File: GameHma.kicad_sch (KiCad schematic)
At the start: 14 parts, among them J1 Screw_Terminal_01x02, J2 Motor_Terminal_01x04, J3 Motor_Terminal_01x04, J4 Motor_Terminal_01x04, J5 Motor_Terminal_01x04, U1 ESP32-DEVKIT-V1, U2 A4988_STEPPER_MOTOR_DRIVER_CA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, U3 A4988_STEPPER_MOTOR_DRIVER_CA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, U4 A4988_STEPPER_MOTOR_DRIVER_CA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, U5 A4988_STEPPER_MOTOR_DRIVER_CA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

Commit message: example of how it's done done done
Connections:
- net Ground: no longer C2.2, J1.2 (Pin_2), U3.15 (GND), U3.9 (GND)
- net Vcc: no longer C2.1, J1.1 (Pin_1), U3.16 (VMOT)
- net at U1.1 (3V3), U2.10 (VDD), U4.10 (VDD)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: no longer U3.10 (VDD)
- net at U1.26 (D14), U2.7 (STEP): now also U1.22 (D33)
- net GND: now reaches U3.1 (~{ENABLE})
- net GND: now also C2.2, J1.2 (Pin_2), U3.15 (GND), U3.9 (GND)
- net at U3.11 (1B): now also J3.2 (Pin_2); no longer J3.1 (Pin_1)
- net at U3.12 (1A): now also J3.1 (Pin_1); no longer J3.3 (Pin_3)
- net at U3.13 (2A): now also J3.3 (Pin_3); no longer J3.2 (Pin_2)
- net +V_{DD}: now reaches U3.2 (MS1)
- net +V_{DD}: now also U3.10 (VDD), U3.3 (MS2), U3.4 (MS3)
- net at U1.23 (D25): no longer U3.7 (STEP)
- net DIR_1: now reaches U3.8 (DIR)
- net DIR_1: no longer U1.22 (D33)
- new net +V_{batt}: C2.1, J1.1 (Pin_1), U3.16 (VMOT)
- new net STEP_1: U3.7 (STEP)
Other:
- moved on the sheet: C2, J1, J3, U3

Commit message: nothing
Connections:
- net Ground is gone; now on net GND: C1.2, C3.2, C4.2, U1.2 (GND), U1.29 (GND), U2.15 (GND), U2.9 (GND), U4.15 (GND), U4.9 (GND), U5.15 (GND), U5.9 (GND)
- net +V_{DD}: now also U1.1 (3V3), U2.10 (VDD), U2.2 (MS1), U2.3 (MS2), U2.4 (MS3), U4.10 (VDD), U4.2 (MS1), U4.3 (MS2), U4.4 (MS3), U5.10 (VDD), U5.2 (MS1), U5.3 (MS2), U5.4 (MS3)
- net +V_{batt}: now also C1.1, C3.1, C4.1, U2.16 (VMOT), U4.16 (VMOT), U5.16 (VMOT)
- net DIR_1: now also U1.25 (D27)
- net GND: now also U2.1 (~{ENABLE}), U4.1 (~{ENABLE}), U5.1 (~{ENABLE})
- net STEP_1: now also U1.26 (D14)
- net at U2.11 (1B): now also J2.2 (Pin_2); no longer J2.1 (Pin_1)
- net at U2.13 (2A): now also J2.3 (Pin_3); no longer J2.2 (Pin_2)
- net at U2.12 (1A): now also J2.1 (Pin_1); no longer J2.3 (Pin_3)
- net DIR_2: now reaches U2.8 (DIR)
- net DIR_2: now also U1.22 (D33); no longer U1.25 (D27)
- net at J5.1 (Pin_1): now also U5.12 (1A); no longer U5.11 (1B)
- net at J5.3 (Pin_3): now also U5.13 (2A); no longer U5.12 (1A)
- net at J5.2 (Pin_2): now also U5.11 (1B); no longer U5.13 (2A)
- net STEP_4: now reaches U1.8 (D5), U5.7 (STEP)
- net DIR_4: now reaches U1.5 (D4), U5.8 (DIR)
- net DIR_3: now reaches U1.10 (D19), U4.8 (DIR)
- net STEP_2: now reaches U1.23 (D25)
- net STEP_2: now also U2.7 (STEP)
- net STEP_3: now reaches U1.9 (D18), U4.7 (STEP)
- net at J4.1 (Pin_1): now also U4.12 (1A); no longer U4.11 (1B)
- net at J4.2 (Pin_2): now also U4.11 (1B); no longer U4.13 (2A)
- net at J4.3 (Pin_3): now also U4.13 (2A); no longer U4.12 (1A)
- removed net Vcc: C1.1, C3.1, C4.1, U1.30 (VIN), U2.16 (VMOT), U4.16 (VMOT), U5.16 (VMOT)
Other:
- moved on the sheet: C2, J1, J3, U3

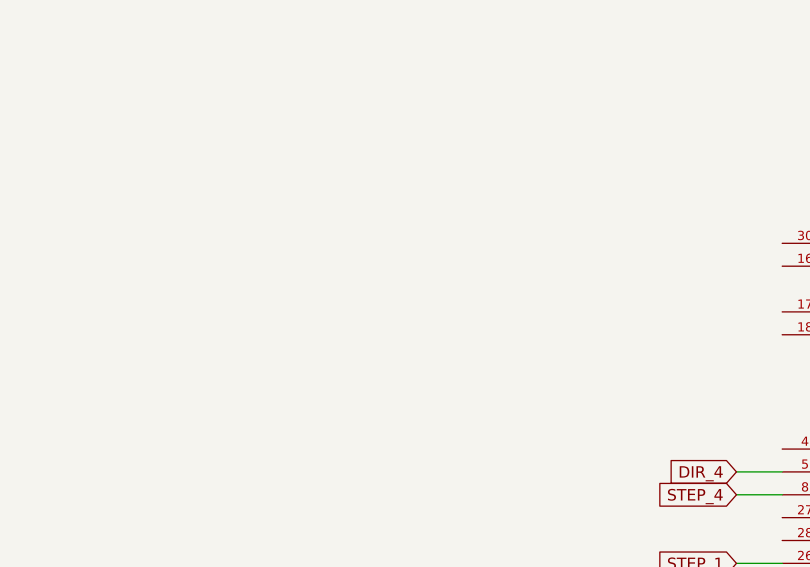
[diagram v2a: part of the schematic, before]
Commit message: create and build SRT_MP1584EN symbol library, add MP1584 in schematic
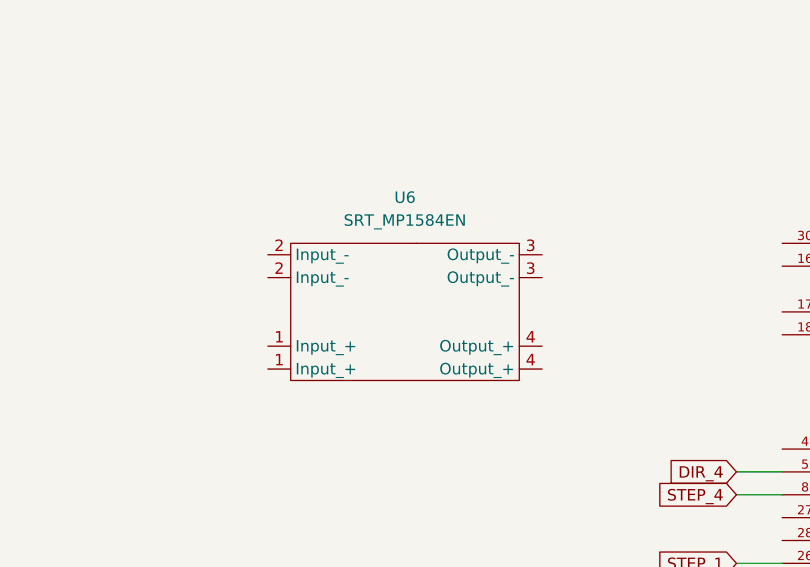
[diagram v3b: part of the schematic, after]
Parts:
- added U6: SRT_MP1584EN, SRT:SRT_MPT1584EN_Module, symbol SRT_MP1584EN:SRT_MP1584EN
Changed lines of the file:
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@@
+	)
+	(symbol
+		(lib_id "SRT_MP1584EN:SRT_MP1584EN")
+		(at 176.53 76.2 0)
+		(unit 1)
+		(exclude_from_sim no)
+		(in_bom yes)
+		(on_board yes)
+		(dnp no)
+		(fields_autoplaced yes)
+		(property "Reference" "U6"
+			(at 175.26 62.23 0)
+			(effects
+				(font
+					(size 1.27 1.27)
+				)
+			)
+		)
+		(property "Value" "SRT_MP1584EN"
+			(at 175.26 64.77 0)
+			(effects
+				(font
+					(size 1.27 1.27)
+				)
+			)
+		)
+		(property "Footprint" "SRT:SRT_MPT1584EN_Module"
+			(at 174.244 102.362 0)
+			(effects
+				(font
+					(size 1.27 1.27)
+				)
+				(hide yes)
+			)
+		)
+		(property "Datasheet" ""
+			(at 176.53 76.2 0)
+			(effects
+				(font
+					(size 1.27 1.27)
+				)
+				(hide yes)
+			)
+		)
+		(property "Description" ""
+			(at 176.53 76.2 0)
+			(effects
+				(font
+					(size 1.27 1.27)
+				)
+				(hide yes)
+			)
+		)
+		(pin "4"
+		)
+		(pin "3"
+		)
+		(pin "1"
+		)
+		(pin "1"
+		)
+		(pin "2"
+		)
+		(pin "2"
+		)
+		(pin "4"
+		)
+		(pin "3"
+		)
+		(instances
+			(project ""
+				(path "/365c5a64-2f06-4047-8707-e000ebaadc48"
+					(reference "U6")
+					(unit 1)
+				)
+			)
+		)
 	)
 	(symbol

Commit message: Organize and add names
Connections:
- net +V_{DD}: now also U6.4 (Output_+)
- net +V_{batt}: now also U6.1 (Input_+)
- net GND: now also U6.2 (Input_-), U6.3 (Output_-)
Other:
- note added: "A4988 STEPPER MOTOR DRIVER CARRIER"
- note added: "Battery"
- note added: "ESP32-DEVKIT-V1"
- note added: "MP1584 Step-Down Buck"
- moved on the sheet: J1, U6

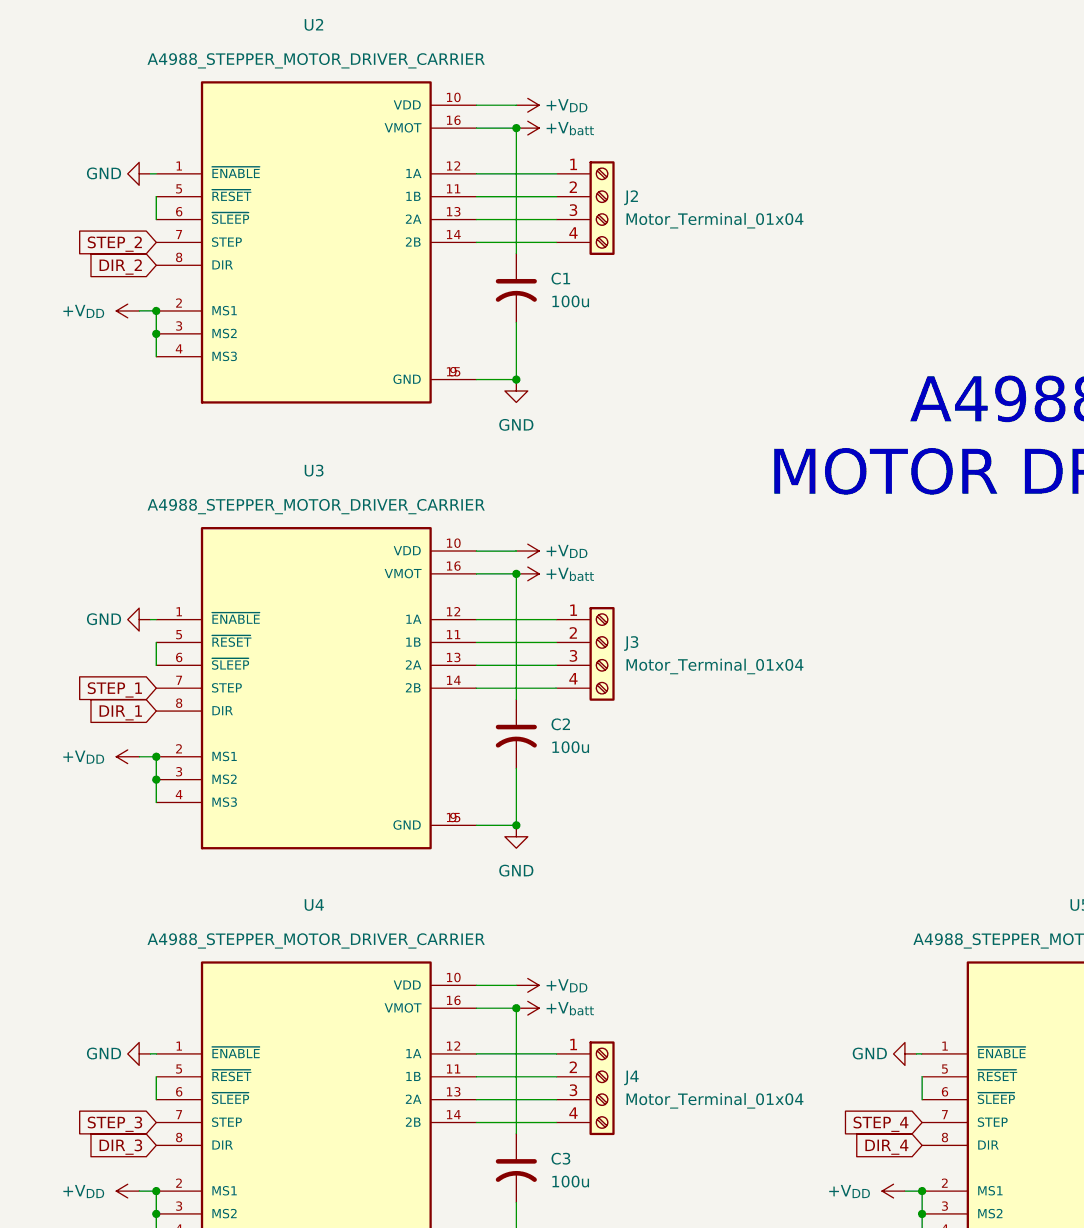
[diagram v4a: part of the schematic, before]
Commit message: add foot print to all companents
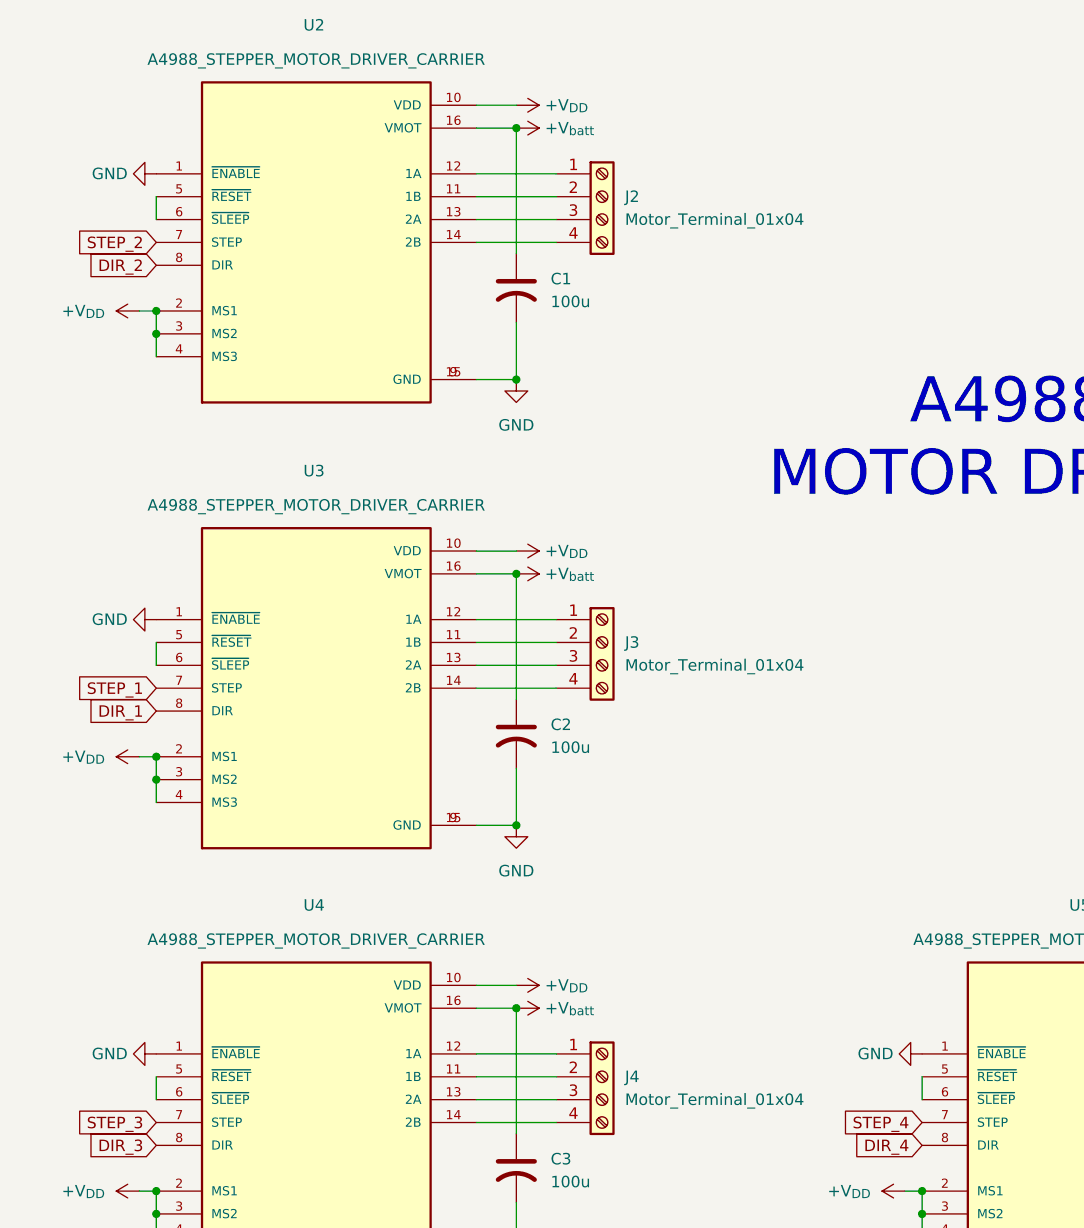
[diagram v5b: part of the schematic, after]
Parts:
- C1, C2, C3, C4: footprint (none) -> Capacitor_THT:C_Radial_D10.0mm_H16.0mm_P5.00mm
- J1: footprint (none) -> TerminalBlock_Phoenix:TerminalBlock_Phoenix_MKDS-1,5-2-5.08_1x02_P5.08mm_Horizontal
- J2, J3, J4, J5: footprint (none) -> Connector_JST:JST_EH_B4B-EH-A_1x04_P2.50mm_Vertical
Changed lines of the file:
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@@
 			(width 0)
 			(type default)
+			(color 0 0 255 1)
 		)
 	)
@@
 			(width 0)
 			(type default)
+			(color 194 0 0 1)
 		)
 	)
@@
 	(wire
 		(pts
-			(xy 27.305 134.62) (xy 27.94 134.62)
-		)
-		(stroke
-			(width 0)
-			(type default)
-		)
-	)
-	(wire
-		(pts
 			(xy 63.5 137.16) (xy 72.39 137.16)
 		)
@@
 			(width 0)
 			(type default)
+			(color 0 0 0 1)
 		)
 	)
@@
 			(width 0)
 			(type default)
-		)
-	)
-	(wire
-		(pts
-			(xy 27.305 86.36) (xy 27.94 86.36)
-		)
-		(stroke
-			(width 0)
-			(type default)
+			(color 0 0 255 1)
 		)
 	)
@@
 	(wire
 		(pts
-			(xy 27.305 36.83) (xy 27.94 36.83)
-		)
-		(stroke
-			(width 0)
-			(type default)
-		)
-	)
-	(wire
-		(pts
 			(xy 63.5 88.9) (xy 72.39 88.9)
 		)
@@
 			(width 0)
 			(type default)
+			(color 0 0 255 1)
 		)
 	)
@@
 			(width 0)
 			(type default)
+			(color 255 0 0 1)
 		)
 	)
@@
 			(width 0)
 			(type default)
+			(color 194 0 0 1)
 		)
 	)
@@
 			(width 0)
 			(type default)
+			(color 194 0 0 1)
 		)
 	)
@@
 	(wire
 		(pts
-			(xy 112.395 134.62) (xy 113.03 134.62)
-		)
-		(stroke
-			(width 0)
-			(type default)
-		)
-	)
-	(wire
-		(pts
 			(xy 226.06 151.13) (xy 231.14 151.13)
 		)
@@
 			(width 0)
 			(type default)
+			(color 194 0 0 1)
 		)
 	)
@@
 			(width 0)
 			(type default)
+			(color 0 0 255 1)
 		)
 	)
@@
 			(width 0)
 			(type default)
+			(color 0 0 0 1)
 		)
 	)
@@
 			)
 		)
-		(property "Footprint" ""
+		(property "Footprint" "Connector_JST:JST_EH_B4B-EH-A_1x04_P2.50mm_Vertical"
 			(at 77.47 137.16 0)
 			(effects
@@
 			)
 		)
-		(property "Footprint" ""
+		(property "Footprint" "Capacitor_THT:C_Radial_D10.0mm_H16.0mm_P5.00mm"
 			(at 67.945 147.32 0)
 			(effects
@@
 	(symbol
 		(lib_id "power:GND")
-		(at 27.305 36.83 270)
+		(at 27.94 36.83 270)
 		(unit 1)
 		(exclude_from_sim no)
@@
 		(fields_autoplaced yes)
 		(property "Reference" "#PWR09"
-			(at 20.955 36.83 0)
+			(at 21.59 36.83 0)
 			(effects
 				(font
@@
 		)
 		(property "Value" "GND"
-			(at 24.13 36.8299 90)
+			(at 24.765 36.8299 90)
 			(effects
 				(font
@@
 		)
 		(property "Footprint" ""
-			(at 27.305 36.83 0)
+			(at 27.94 36.83 0)
 			(effects
 				(font
@@
 		)
 		(property "Datasheet" ""
-			(at 27.305 36.83 0)
+			(at 27.94 36.83 0)
 			(effects
 				(font
@@
 		)
 		(property "Description" "Power symbol creates a global label with name \"GND\" , ground"
-			(at 27.305 36.83 0)
+			(at 27.94 36.83 0)
 			(effects
 				(font
@@
 			)
 		)
-		(property "Footprint" ""
+		(property "Footprint" "Capacitor_THT:C_Radial_D10.0mm_H16.0mm_P5.00mm"
 			(at 67.945 49.53 0)
 			(effects
@@
 	(symbol
 		(lib_id "power:GND")
-		(at 27.305 86.36 270)
+		(at 27.94 86.36 270)
 		(unit 1)
 		(exclude_from_sim no)
@@
 		(fields_autoplaced yes)
 		(property "Reference" "#PWR04"
-			(at 20.955 86.36 0)
+			(at 21.59 86.36 0)
 			(effects
 				(font
@@
 		)
 		(property "Value" "GND"
-			(at 24.13 86.3599 90)
+			(at 24.765 86.3599 90)
 			(effects
 				(font
@@
 		)
 		(property "Footprint" ""
-			(at 27.305 86.36 0)
+			(at 27.94 86.36 0)
 			(effects
 				(font
@@
 		)
 		(property "Datasheet" ""
-			(at 27.305 86.36 0)
+			(at 27.94 86.36 0)
 			(effects
 				(font
@@
 		)
 		(property "Description" "Power symbol creates a global label with name \"GND\" , ground"
-			(at 27.305 86.36 0)
+			(at 27.94 86.36 0)
 			(effects
 				(font
@@
 			)
 		)
-		(property "Footprint" ""
+		(property "Footprint" "TerminalBlock_Phoenix:TerminalBlock_Phoenix_MKDS-1,5-2-5.08_1x02_P5.08mm_Horizontal"
 			(at 243.84 39.37 0)
 			(effects
@@
 			)
 		)
-		(property "Footprint" ""
+		(property "Footprint" "Connector_JST:JST_EH_B4B-EH-A_1x04_P2.50mm_Vertical"
 			(at 77.47 39.37 0)
 			(effects
@@
 			)
 		)
-		(property "Footprint" ""
+		(property "Footprint" "Capacitor_THT:C_Radial_D10.0mm_H16.0mm_P5.00mm"
 			(at 153.035 147.32 0)
 			(effects
@@
 			)
 		)
-		(property "Footprint" ""
+		(property "Footprint" "Capacitor_THT:C_Radial_D10.0mm_H16.0mm_P5.00mm"
 			(at 67.945 99.06 0)
 			(effects
@@
 			)
 		)
-		(property "Footprint" ""
+		(property "Footprint" "Connector_JST:JST_EH_B4B-EH-A_1x04_P2.50mm_Vertical"
 			(at 162.56 137.16 0)
 			(effects
@@
 	(symbol
 		(lib_id "power:GND")
-		(at 27.305 134.62 270)
+		(at 27.94 134.62 270)
 		(unit 1)
 		(exclude_from_sim no)
@@
 		(fields_autoplaced yes)
 		(property "Reference" "#PWR014"
-			(at 20.955 134.62 0)
+			(at 21.59 134.62 0)
 			(effects
 				(font
@@
 		)
 		(property "Value" "GND"
-			(at 24.13 134.6199 90)
+			(at 24.765 134.6199 90)
 			(effects
 				(font
@@
 		)
 		(property "Footprint" ""
-			(at 27.305 134.62 0)
+			(at 27.94 134.62 0)
 			(effects
 				(font
@@
 		)
 		(property "Datasheet" ""
-			(at 27.305 134.62 0)
+			(at 27.94 134.62 0)
 			(effects
 				(font
@@
 		)
 		(property "Description" "Power symbol creates a global label with name \"GND\" , ground"
-			(at 27.305 134.62 0)
+			(at 27.94 134.62 0)
 			(effects
 				(font
@@
 			)
 		)
-		(property "Footprint" ""
+		(property "Footprint" "Connector_JST:JST_EH_B4B-EH-A_1x04_P2.50mm_Vertical"
 			(at 77.47 88.9 0)
 			(effects
@@
 	(symbol
 		(lib_id "power:GND")
-		(at 112.395 134.62 270)
+		(at 113.03 134.62 270)
 		(unit 1)
 		(exclude_from_sim no)
@@
 		(fields_autoplaced yes)
 		(property "Reference" "#PWR019"
-			(at 106.045 134.62 0)
+			(at 106.68 134.62 0)
 			(effects
 				(font
@@
 		)
 		(property "Value" "GND"
-			(at 109.22 134.6199 90)
+			(at 109.855 134.6199 90)
 			(effects
 				(font
@@
 		)
 		(property "Footprint" ""
-			(at 112.395 134.62 0)
+			(at 113.03 134.62 0)
 			(effects
 				(font
@@
 		)
 		(property "Datasheet" ""
-			(at 112.395 134.62 0)
+			(at 113.03 134.62 0)
 			(effects
 				(font
@@
 		)
 		(property "Description" "Power symbol creates a global label with name \"GND\" , ground"
-			(at 112.395 134.62 0)
+			(at 113.03 134.62 0)
 			(effects
 				(font
